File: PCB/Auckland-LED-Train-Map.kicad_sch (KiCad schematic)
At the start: 96 parts, among them J1 Prog Connector, Q1 HL3415A, Q2 MMBT3904, U1 XC6206P332MR, U2 ESP32-C3FH4, U3 SN74LVC4245APWR, U4 Connector, USB-TYPE-C-16P, U5 Connector, USB-TYPE-C-16P, X1 40MHz, 15pF

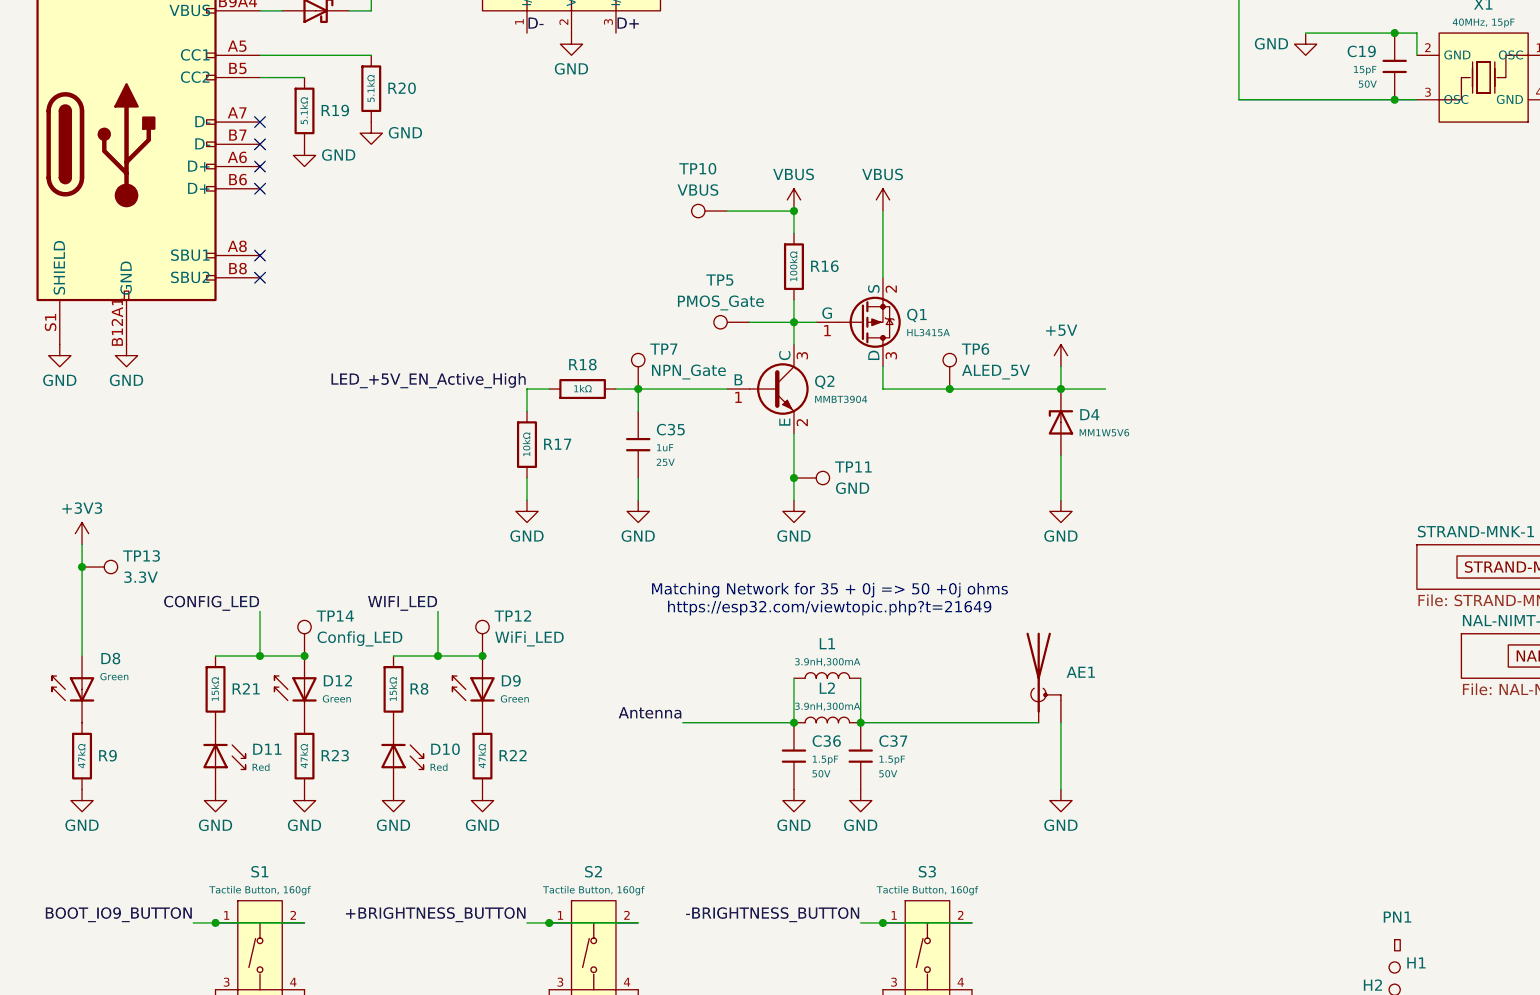
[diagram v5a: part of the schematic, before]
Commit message: Fix charlieplexed LEDs D10 and D11
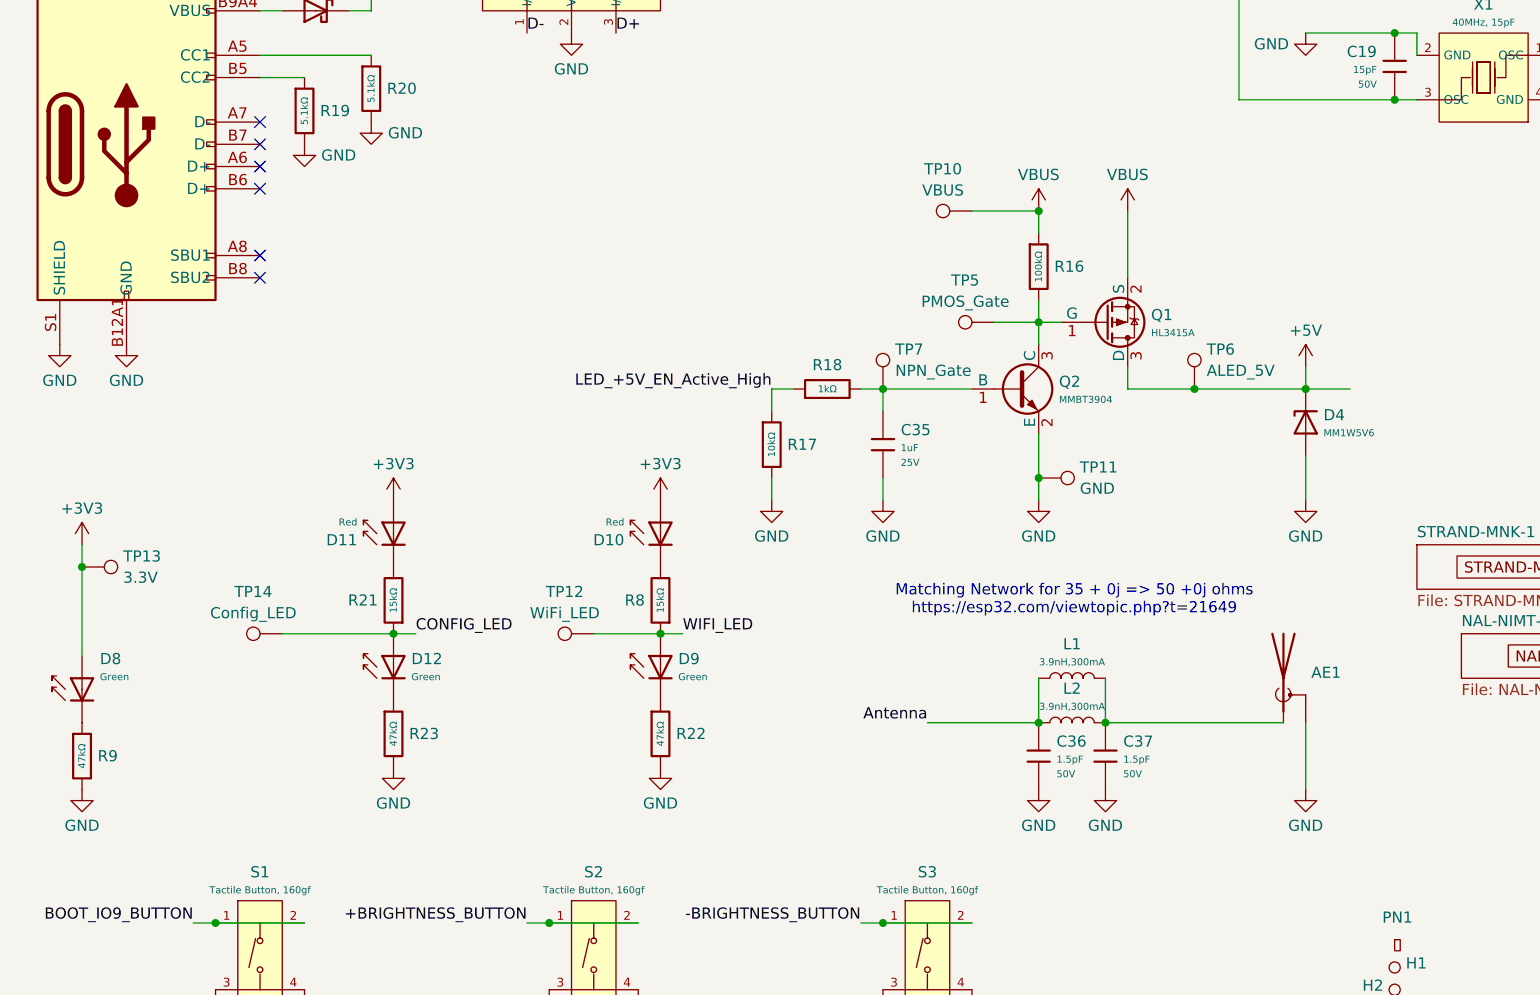
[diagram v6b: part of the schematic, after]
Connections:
- net +3V3: now also D10.2, D11.2
- net GND: no longer D10.2, D11.2
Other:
- moved on the sheet: AE1, C35, C36, C37, D10, D11, D12, D4, D9, L1, L2, Q1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

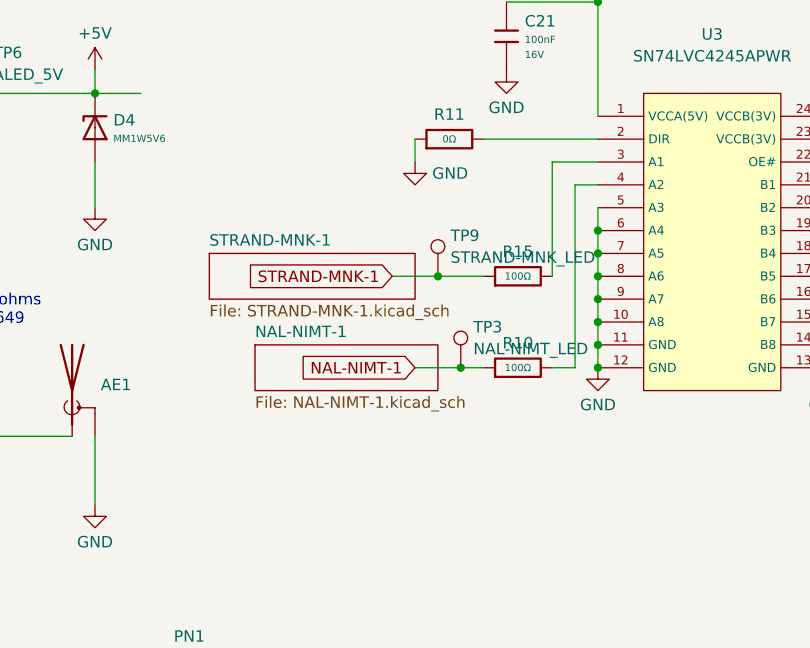
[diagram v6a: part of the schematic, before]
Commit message: Add changes suggested from reddit
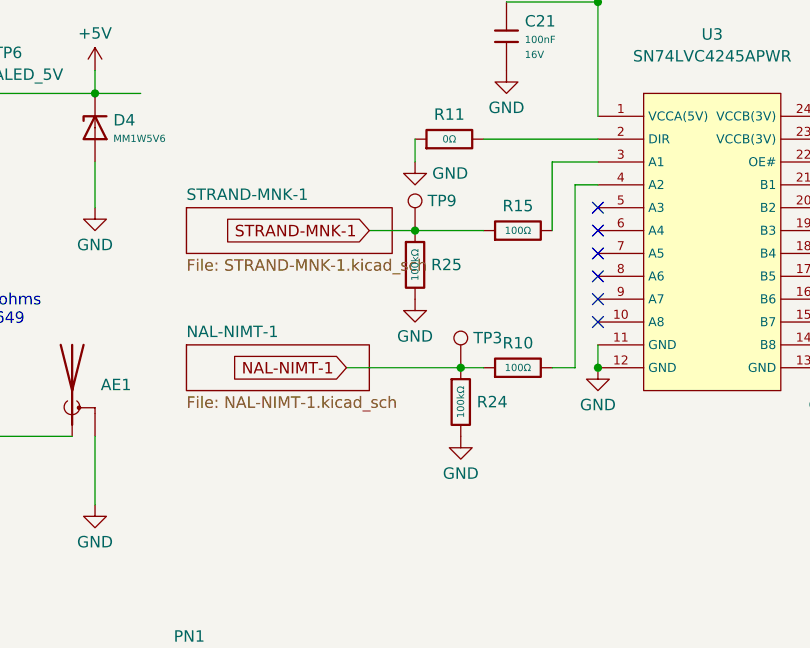
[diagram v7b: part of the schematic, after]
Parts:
- added R24, R25: 100kΩ, PCM_JLCPCB:R_0402, symbol PCM_JLCPCB-Resistors:0402,100kΩ
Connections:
- net GND: now also R24.2, R25.2; no longer U3.10 (A8), U3.5 (A3), U3.6 (A4), U3.7 (A5), U3.8 (A6), U3.9 (A7)
- net NAL-NIMT-1: now also R24.1
- net STRAND-MNK-1: now also R25.1
- no-connect marks 14 -> 20
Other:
- moved on the sheet: R15, TP9

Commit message: Final tweaks for V1.0.0
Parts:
- removed C15: 100nF, PCM_JLCPCB:C_0402, symbol PCM_JLCPCB-Capacitors:0402,100nF
- removed C19, C20: 15pF, PCM_JLCPCB:C_0402, symbol PCM_JLCPCB-Capacitors:0402,15pF
- removed C5: 10uF, PCM_JLCPCB:C_0402, symbol PCM_JLCPCB-Capacitors:0402,10uF
- removed L1, L4: 3.9nH,300mA, PCM_JLCPCB:L_0402, symbol PCM_JLCPCB-Inductors:3.9nH,300mA
- added C15, C5: 100uF, PCM_JLCPCB:C_1206, symbol PCM_JLCPCB-Capacitors:1206,100uF
- added C17: 100nF, PCM_JLCPCB:C_0402, symbol PCM_JLCPCB-Capacitors:0402,100nF
- added C19, C20: 27pF, PCM_JLCPCB:C_0402, symbol PCM_JLCPCB-Capacitors:0402,27pF
- added C23, C24: C_Small, PCM_JLCPCB:C_0402, symbol Device:C_Small
- added C25: 10uF, PCM_JLCPCB:C_0603, symbol PCM_JLCPCB-Capacitors:0603,10uF
- added D13: H3V3U10B, PCM_JLCPCB:D_DFN1006-2L, symbol PCM_JLCPCB-Diodes:TVS-Bi,H3V3U10B
- added R26: 0Ω, PCM_JLCPCB:R_0402, symbol PCM_JLCPCB-Resistors:0402,0Ω
- AE1, H1, H2, H3, H4, J1, PN1, TP10, TP11, TP12, TP13, TP14, TP15, TP2, TP3, TP5, TP6, TP7, TP8, TP9: now left out of the parts list
- C36, C37: Stock 119360 -> 87496
- F1: value Polyfuse -> Polyfuse, 2.5A; LCSC (none) -> C2757931; Manufacturer (none) -> BHFUSE; Part (none) -> BSMD0805L-200; Process (none) -> SMT
- L1: renamed from L2; value 3.9nH,300mA -> 2.7nH; Attrition Qty 10 -> (none); Category Inductors/Coils/Transformers,Inductors (SMD) -> (none); Class Preferred Component -> (none); DC Resistance (DCR) 200mΩ -> (none); Frequency - Self Resonant 4GHz -> (none); Inductance 3.9nH -> (none); LCSC C14033 -> C77108; Manufacturer Sunlord -> Murata Electronics; Minimum Qty 20 -> (none); Part SDCL1005C3N9STDF -> LQG15HS2N7S02D; Price 0.007USD -> (none); Q @ Freq 8@100MHz -> (none); Rated Current 300mA -> (none); Stock 55146 -> (none)
- L3: value 3.9nH,300mA -> 2.7nH; Attrition Qty 10 -> (none); Category Inductors/Coils/Transformers,Inductors (SMD) -> (none); Class Preferred Component -> (none); DC Resistance (DCR) 200mΩ -> (none); Frequency - Self Resonant 4GHz -> (none); Inductance 3.9nH -> (none); LCSC C14033 -> C77108; Manufacturer Sunlord -> Murata Electronics; Minimum Qty 20 -> (none); Part SDCL1005C3N9STDF -> LQG15HS2N7S02D; Price 0.007USD -> (none); Q @ Freq 8@100MHz -> (none); Rated Current 300mA -> (none); Stock 55146 -> (none)
- U2: footprint PCM_JLCPCB:QFN-32-1EP_5x5mm_P0.5mm_EP3.7x3.7mm_ThermalVias -> Custom_Footprints:QFN-32-1EP_5x5mm_P0.5mm_EP3.7x3.7mm_ThermalVias; Manufacturer (none) -> Espressif Systems; Part (none) -> ESP32-C3FH4; Process (none) -> SMT
- U4, U5: Manufacturer (none) -> DEALON; Part (none) -> USB-TYPE-C-019; Process (none) -> SMT
- X1: footprint PCM_JLCPCB:OSC-SMD_4P-L3.2-W2.5-BL_SIT8008BI -> Custom_Footprints:OSC-SMD_4P-L3.2-W2.5-BL_SIT8008BI; Manufacturer (none) -> YXC Crystal Oscillators; Part (none) -> X322540MPB4SI; PartID X322540MPB4SI -> (none); Process (none) -> SMT
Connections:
- net +3V3: now also C15.1, C5.1
- net Antenna: now also D13.2
- net D+: now also C23.1
- net D-: now also C24.1
- net GND: now also C15.2, C17.2, C19.1, C20.2, C23.2, C24.2, C25.2, C5.2, D13.1
- net Reset: now also R26.2; no longer U2.7 (CHIP_EN)
- net VBUS: now also C25.1
- net at L5.1, X1.1 (OSC): now also C20.1
- net at U2.29 (XTAL_N), X1.3 (OSC): now also C19.2
- new net: C17.1, R26.1, U2.7 (CHIP_EN)
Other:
- moved on the sheet: C14, C6, C7, C8, D1, D5, R13, R14, R4
